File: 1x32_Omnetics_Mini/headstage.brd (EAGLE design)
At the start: 100 x 80 mm, 13 parts, among them U1 RHD2132_QFN

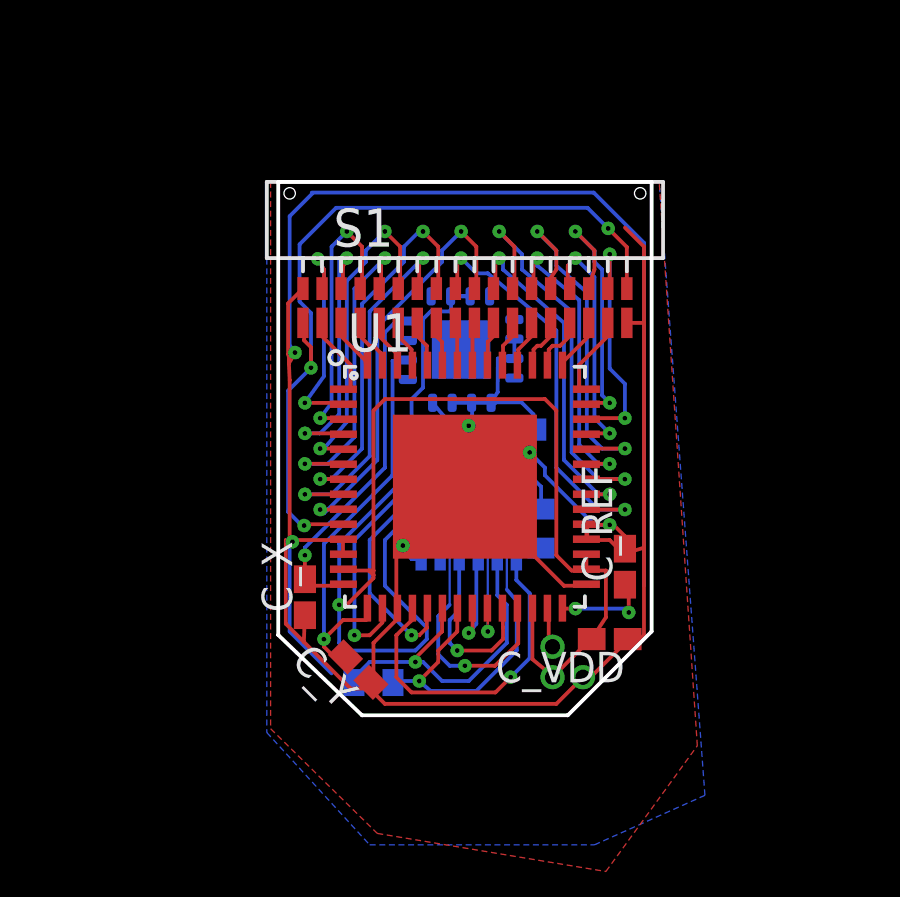
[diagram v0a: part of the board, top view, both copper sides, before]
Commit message: fixed tolerances
ran DRC with the high end-ish advanced circuit specs (2.75mil
width/spacing, 6mil drill) and fixed things. Still getting some errors
but its closer to viable now.
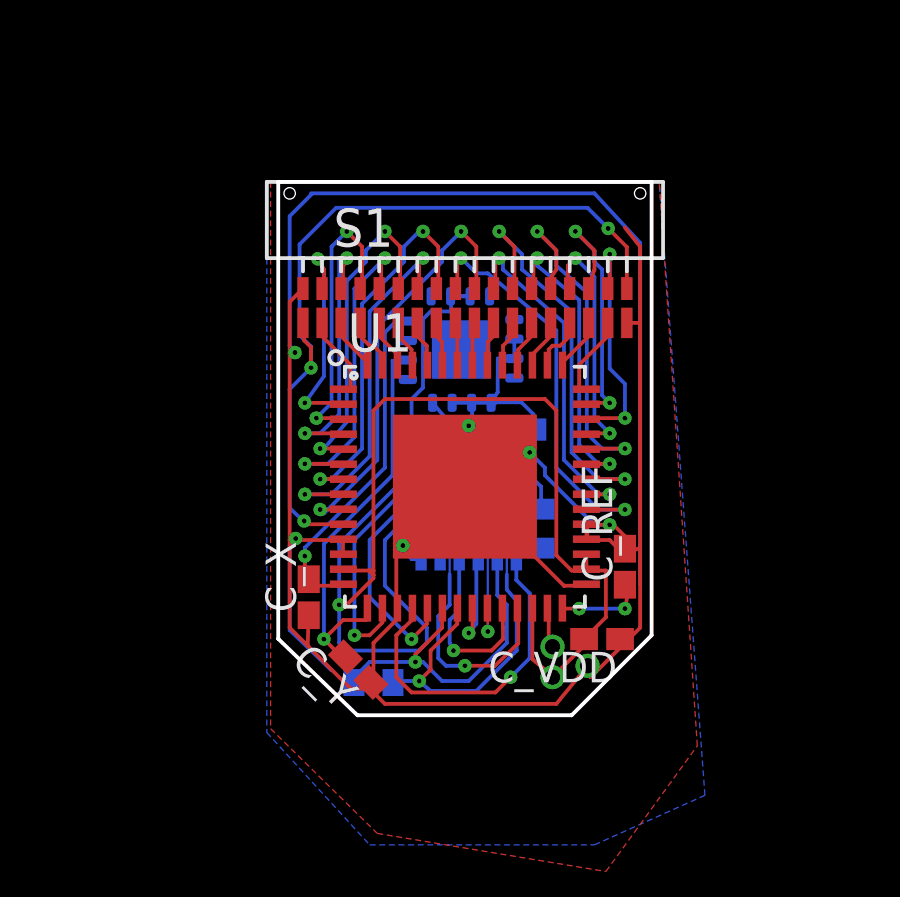
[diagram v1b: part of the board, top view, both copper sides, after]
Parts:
- moved C_VDD 0.25 mm to (22.4, 14.0)
- moved C_X 0.13 mm to (12.6, 15.4)
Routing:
- net N$2: track 4.90 -> 0.00 mm
- net GND: track 101.9 -> 106.6 mm
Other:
- outline, holes or cut-outs redrawn

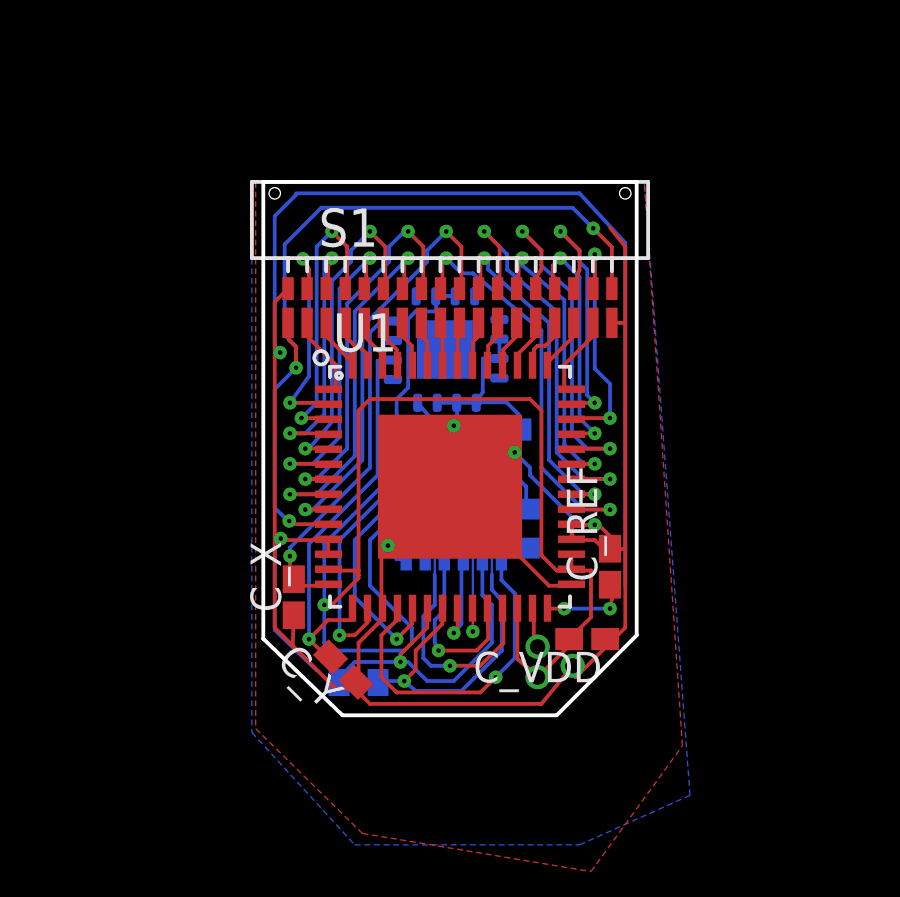
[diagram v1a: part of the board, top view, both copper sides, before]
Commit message: added ref via, more cleanup
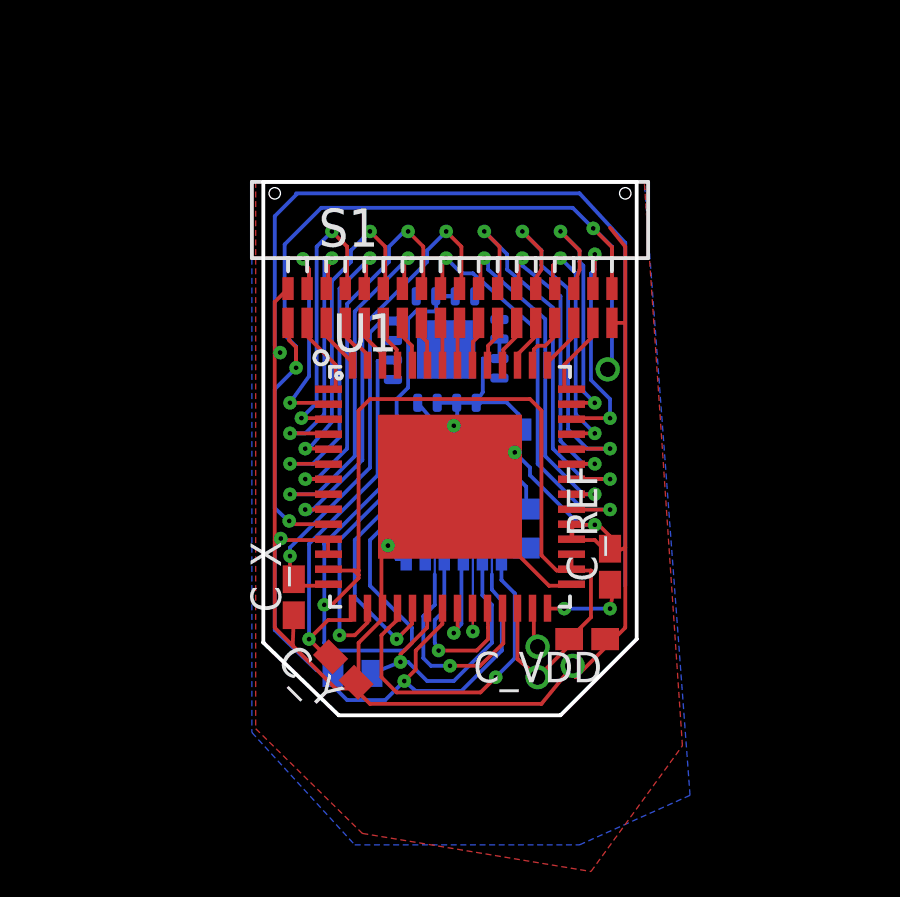
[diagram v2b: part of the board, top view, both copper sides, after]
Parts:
- moved R2 0.37 mm to (14.5, 12.8), turned to 0 degrees
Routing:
- net N$1: track 5.72 -> 0.00 mm
- net GND: track 106.6 -> 112.0 mm
- net REF: track 26.2 -> 31.3 mm, vias 3 -> 4
- net SCLK+: track 12.3 -> 14.7 mm
- net SCLK-: track 11.6 -> 9.95 mm
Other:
- outline, holes or cut-outs redrawn
- board text added: "aux"
- board text added: "gnd"
- board text added: "ref"
- board text added: "vdd"
- board text removed: "mini"

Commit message: some cleanups
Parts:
- moved R2 0.13 mm to (14.5, 13.0)
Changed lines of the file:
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@@
 <?xml version="1.0" encoding="utf-8"?>
 <!DOCTYPE eagle SYSTEM "eagle.dtd">
-<eagle version="7.5.0">
+<eagle version="6.3">
 <drawing>
 <settings>
@@
 <setting verticaltext="up"/>
 </settings>
-<grid distance="1" unitdist="mil" unit="mil" style="lines" multiple="1" display="yes" altdistance="0.025" altunitdist="inch" altunit="inch"/>
+<grid distance="5" unitdist="mil" unit="mil" style="lines" multiple="1" display="yes" altdistance="0.025" altunitdist="inch" altunit="inch"/>
 <layers>
 <layer number="1" name="Top" color="12" fill="1" visible="yes" active="yes"/>
@@
 <pass name="Default">
 <param name="RoutingGrid" value="50mil"/>
-<param name="AutoGrid" value="1"/>
-<param name="Efforts" value="0"/>
-<param name="TopRouterVariant" value="1"/>
 <param name="tpViaShape" value="round"/>
 <param name="PrefDir.1" value="|"/>
@@
 <element name="U1" library="RHD2000" package="QFN56_8_X_8_LARGE" value="RHD2132_QFN" x="17.78" y="19.05"/>
 <element name="R1" library="resistor" package="R0402" value="100" x="20.32" y="17.653" rot="MR90"/>
-<element name="R2" library="resistor" package="R0402" value="100" x="14.5288" y="12.827" rot="MR0"/>
+<element name="R2" library="resistor" package="R0402" value="100" x="14.5288" y="12.954" rot="MR0"/>
 <element name="R3" library="resistor" package="R0402" value="100" x="18.415" y="19.177" rot="MR180"/>
 <element name="C_A" library="resistor" package="C0402K" value="0.1uF" x="16.51" y="20.32" rot="MR270"/>
@@
 <contactref element="U1" pad="18"/>
 <wire x1="19.558" y1="16.5735" x2="19.4945" y2="16.637" width="0.127" layer="16"/>
-<wire x1="19.4945" y1="16.637" x2="19.4945" y2="15.9385" width="0.127" layer="16"/>
+<wire x1="19.4945" y1="16.637" x2="19.4945" y2="16.1925" width="0.127" layer="16"/>
 <wire x1="20.32" y1="17.003" x2="19.5095" y2="16.876" width="0.127" layer="16"/>
 <wire x1="19.5095" y1="16.876" x2="19.4945" y2="16.637" width="0.0762" layer="16"/>
-<wire x1="19.4945" y1="15.9385" x2="19.939" y2="15.494" width="0.127" layer="16"/>
-<wire x1="19.939" y1="15.494" x2="19.939" y2="13.335" width="0.127" layer="16"/>
+<wire x1="19.4945" y1="16.1925" x2="19.939" y2="15.748" width="0.127" layer="16"/>
+<wire x1="19.939" y1="15.748" x2="19.939" y2="13.335" width="0.127" layer="16"/>
 <wire x1="19.939" y1="13.335" x2="19.304" y2="12.7" width="0.127" layer="16"/>
 <via x="19.304" y="12.7" extent="1-16" drill="0.1524"/>
@@
 <wire x1="17.03" y1="15" x2="17.03" y2="14.871" width="0.127" layer="1"/>
 <wire x1="17.03" y1="14.871" x2="17.018" y2="14.859" width="0.127" layer="1"/>
-<wire x1="16.129" y1="13.208" x2="15.1788" y2="12.827" width="0.127" layer="16"/>
+<wire x1="16.129" y1="13.208" x2="15.1788" y2="12.954" width="0.127" layer="16"/>
 </signal>
 <signal name="SCLK+">
@@
 <contactref element="U1" pad="21"/>
 <contactref element="R2" pad="2"/>
-<wire x1="18.8595" y1="17.78" x2="19.05" y2="17.78" width="0.0762" layer="16"/>
-<wire x1="19.05" y1="17.78" x2="19.177" y2="17.653" width="0.0762" layer="16"/>
-<wire x1="19.177" y1="17.653" x2="19.177" y2="16.129" width="0.0762" layer="16"/>
+<wire x1="18.8595" y1="17.78" x2="19.05" y2="17.2466" width="0.0762" layer="16"/>
+<wire x1="19.05" y1="17.2466" x2="19.177" y2="17.1196" width="0.0762" layer="16"/>
+<wire x1="19.177" y1="17.1196" x2="19.177" y2="16.129" width="0.0762" layer="16"/>
 <wire x1="19.177" y1="16.129" x2="19.177" y2="15.621" width="0.127" layer="16"/>
 <wire x1="19.177" y1="15.621" x2="19.5072" y2="15.24" width="0.127" layer="16"/>
@@
 <wire x1="17.526" y1="14.605" x2="17.526" y2="14.996" width="0.0762" layer="1"/>
 <wire x1="17.526" y1="14.996" x2="17.53" y2="15" width="0.0762" layer="1"/>
-<wire x1="16.256" y1="12.573" x2="15.621" y2="11.938" width="0.127" layer="16"/>
-<wire x1="15.621" y1="11.938" x2="14.351" y2="11.938" width="0.127" layer="16"/>
-<wire x1="14.351" y1="11.938" x2="14.0058" y2="12.2832" width="0.127" layer="16"/>
-<wire x1="14.0058" y1="12.2832" x2="13.8788" y2="12.827" width="0.127" layer="16"/>
+<wire x1="16.256" y1="12.573" x2="16.002" y2="12.319" width="0.127" layer="16"/>
+<wire x1="16.002" y1="12.319" x2="14.097" y2="12.319" width="0.127" layer="16"/>
+<wire x1="14.097" y1="12.319" x2="13.8788" y2="12.5372" width="0.127" layer="16"/>
+<wire x1="13.8788" y1="12.5372" x2="13.8788" y2="12.954" width="0.127" layer="16"/>
 </signal>
 <signal name="MOSI+">
@@
 <contactref element="R3" pad="2"/>
 <wire x1="18.2245" y1="17.78" x2="18.161" y2="17.653" width="0.127" layer="16"/>
-<wire x1="18.161" y1="17.653" x2="18.415" y2="17.653" width="0.0762" layer="16"/>
-<wire x1="18.415" y1="17.653" x2="18.542" y2="17.526" width="0.0762" layer="16"/>
-<wire x1="18.542" y1="17.526" x2="18.542" y2="14.224" width="0.0762" layer="16"/>
+<wire x1="18.161" y1="17.653" x2="18.415" y2="17.2212" width="0.0762" layer="16"/>
+<wire x1="18.415" y1="17.2212" x2="18.542" y2="17.0942" width="0.0762" layer="16"/>
+<wire x1="18.542" y1="17.0942" x2="18.542" y2="14.224" width="0.0762" layer="16"/>
 <via x="18.542" y="14.224" extent="1-16" drill="0.1524"/>
 <wire x1="18.542" y1="14.224" x2="18.542" y2="14.859" width="0.0762" layer="1"/>
@@
 <wire x1="17.765" y1="19.177" x2="17.892" y2="19.065" width="0.0762" layer="16"/>
 <wire x1="17.892" y1="19.065" x2="17.907" y2="18.415" width="0.127" layer="16"/>
-<wire x1="17.907" y1="18.415" x2="17.907" y2="16.9545" width="0.0762" layer="16"/>
-<wire x1="17.907" y1="16.9545" x2="18.2245" y2="16.637" width="0.0762" layer="16"/>
+<wire x1="17.907" y1="18.415" x2="17.907" y2="17.145" width="0.0762" layer="16"/>
+<wire x1="17.907" y1="17.145" x2="18.2118" y2="16.8402" width="0.0762" layer="16"/>
+<wire x1="18.2118" y1="16.8402" x2="18.2245" y2="16.637" width="0.0762" layer="16"/>
 <wire x1="18.03" y1="15" x2="18.03" y2="14.9392" width="0.127" layer="1"/>
 <wire x1="18.03" y1="14.9392" x2="18.034" y2="14.9352" width="0.127" layer="1"/>
@@
 <contactref element="S2" pad="B4"/>
 <contactref element="U1" pad="24"/>
-<wire x1="17.5895" y1="16.637" x2="17.5895" y2="14.9225" width="0.127" layer="16"/>
-<wire x1="17.5895" y1="14.9225" x2="17.272" y2="14.605" width="0.127" layer="16"/>
-<wire x1="17.272" y1="14.605" x2="17.272" y2="13.843" width="0.127" layer="16"/>
+<wire x1="17.5895" y1="16.637" x2="17.5895" y2="14.6685" width="0.127" layer="16"/>
+<wire x1="17.5895" y1="14.6685" x2="17.272" y2="14.351" width="0.127" layer="16"/>
+<wire x1="17.272" y1="14.351" x2="17.272" y2="13.843" width="0.127" layer="16"/>
 <wire x1="17.272" y1="13.843" x2="17.399" y2="13.589" width="0.127" layer="16"/>
 <via x="17.399" y="13.589" extent="1-16" drill="0.1524"/>
@@
 <contactref element="U1" pad="25"/>
 <contactref element="S2" pad="T4"/>
-<wire x1="17.5895" y1="17.78" x2="17.526" y2="17.78" width="0.0762" layer="16"/>
-<wire x1="17.526" y1="17.78" x2="17.272" y2="17.653" width="0.0762" layer="16"/>
-<wire x1="17.272" y1="17.653" x2="17.272" y2="16.129" width="0.0762" layer="16"/>
-<wire x1="17.272" y1="16.129" x2="17.272" y2="15.113" width="0.127" layer="16"/>
-<wire x1="17.272" y1="15.113" x2="16.891" y2="14.732" width="0.127" layer="16"/>
-<wire x1="16.891" y1="14.732" x2="16.891" y2="13.335" width="0.127" layer="16"/>
+<wire x1="17.5895" y1="17.78" x2="17.526" y2="17.2974" width="0.0762" layer="16"/>
+<wire x1="17.526" y1="17.2974" x2="17.272" y2="17.1704" width="0.0762" layer="16"/>
+<wire x1="17.272" y1="17.1704" x2="17.272" y2="16.129" width="0.0762" layer="16"/>
+<wire x1="17.272" y1="16.129" x2="17.272" y2="14.859" width="0.127" layer="16"/>
+<wire x1="17.272" y1="14.859" x2="16.891" y2="14.478" width="0.127" layer="16"/>
+<wire x1="16.891" y1="14.478" x2="16.891" y2="13.335" width="0.127" layer="16"/>
 <wire x1="16.891" y1="13.335" x2="17.145" y2="13.081" width="0.127" layer="16"/>
 <wire x1="17.145" y1="13.081" x2="17.78" y2="13.081" width="0.127" layer="16"/>
@@
 <via x="12.446" y="21.844" extent="1-16" drill="0.1524"/>
 <wire x1="13.686" y1="21.844" x2="12.446" y2="21.844" width="0.127" layer="1"/>
-<wire x1="13.081" y1="26.289" x2="13.081" y2="22.733" width="0.127" layer="16"/>
-<wire x1="13.081" y1="22.733" x2="12.446" y2="21.844" width="0.127" layer="16"/>
+<wire x1="13.081" y1="26.289" x2="13.081" y2="22.479" width="0.127" layer="16"/>
+<wire x1="13.081" y1="22.479" x2="12.446" y2="21.844" width="0.127" layer="16"/>
 <contactref element="U1" pad="2"/>
 <contactref element="S1" pad="B2"/>
@@
 <wire x1="14.478" y1="26.924" x2="14.478" y2="26.543" width="0.127" layer="16"/>
 <wire x1="14.478" y1="26.543" x2="13.843" y2="25.908" width="0.127" layer="16"/>
-<wire x1="13.843" y1="25.908" x2="13.843" y2="21.209" width="0.127" layer="16"/>
+<wire x1="13.843" y1="25.908" x2="13.843" y2="21.082" width="0.127" layer="16"/>
 <via x="12.954" y="20.32" extent="1-16" drill="0.1524"/>
 <wire x1="12.954" y1="20.32" x2="13.081" y2="20.32" width="0.127" layer="16"/>
-<wire x1="13.081" y1="20.32" x2="13.843" y2="21.209" width="0.127" layer="16"/>
+<wire x1="13.081" y1="20.32" x2="13.843" y2="21.082" width="0.127" layer="16"/>
 <contactref element="U1" pad="5"/>
 <contactref element="S1" pad="B6"/>
@@
 <wire x1="13.843" y1="26.543" x2="13.843" y2="26.67" width="0.127" layer="1"/>
 <wire x1="12.446" y1="20.828" x2="12.954" y2="20.828" width="0.127" layer="16"/>
-<wire x1="13.843" y1="26.67" x2="13.589" y2="26.67" width="0.127" layer="16"/>
-<wire x1="13.589" y1="26.67" x2="13.589" y2="21.463" width="0.127" layer="16"/>
+<wire x1="13.843" y1="26.67" x2="13.589" y2="26.416" width="0.127" layer="16"/>
+<wire x1="13.589" y1="26.416" x2="13.589" y2="21.463" width="0.127" layer="16"/>
 <wire x1="13.589" y1="21.463" x2="12.954" y2="20.828" width="0.127" layer="16"/>
 <contactref element="U1" pad="4"/>
